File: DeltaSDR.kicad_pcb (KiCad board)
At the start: 2 copper layers, 168 parts, among them J1 Conn_01x03_Male, J2 Conn_01x05_Male, J3 Barrel_Jack, J4 USB_A, J5 Conn_Coaxial, Q1 BSS123, Q2 BSS123, Q3 BSS123, Q4 BSS123, Q5 BSS123, Q6 BSS123, T1 Transformer_1P_SS, T2 Transformer_1P_SS, U1 TC1262-33, U10 TLV2464CD, U11 SN74CBT3253, U12 MMG3H21NT1, U2 Si570, U3 SN74CBT3253, U4 PCM3060, U5 CY8C3246PVI-147, U6 TLV761, U7 TLV761, U8 74HC74, U9 LT6231CSB, Y1 Crystal_GND24

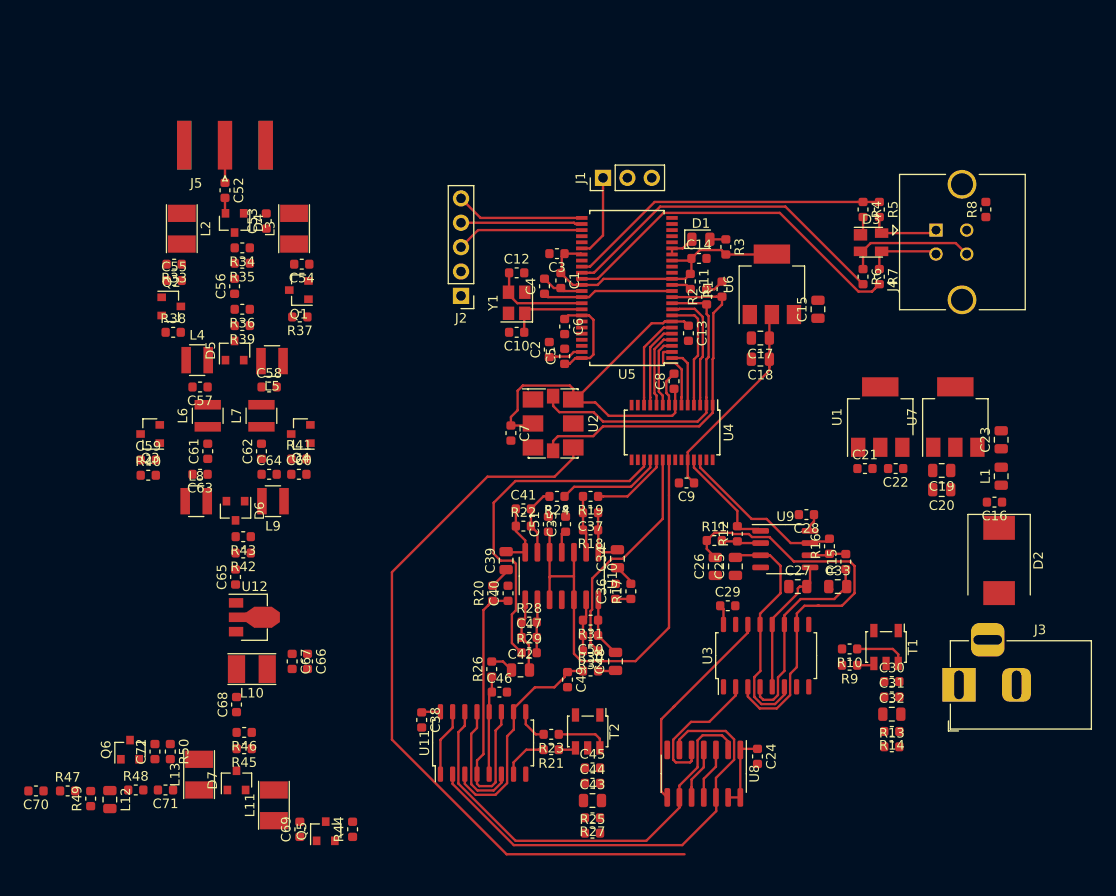
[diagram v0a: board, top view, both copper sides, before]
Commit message: Layout: All components connected
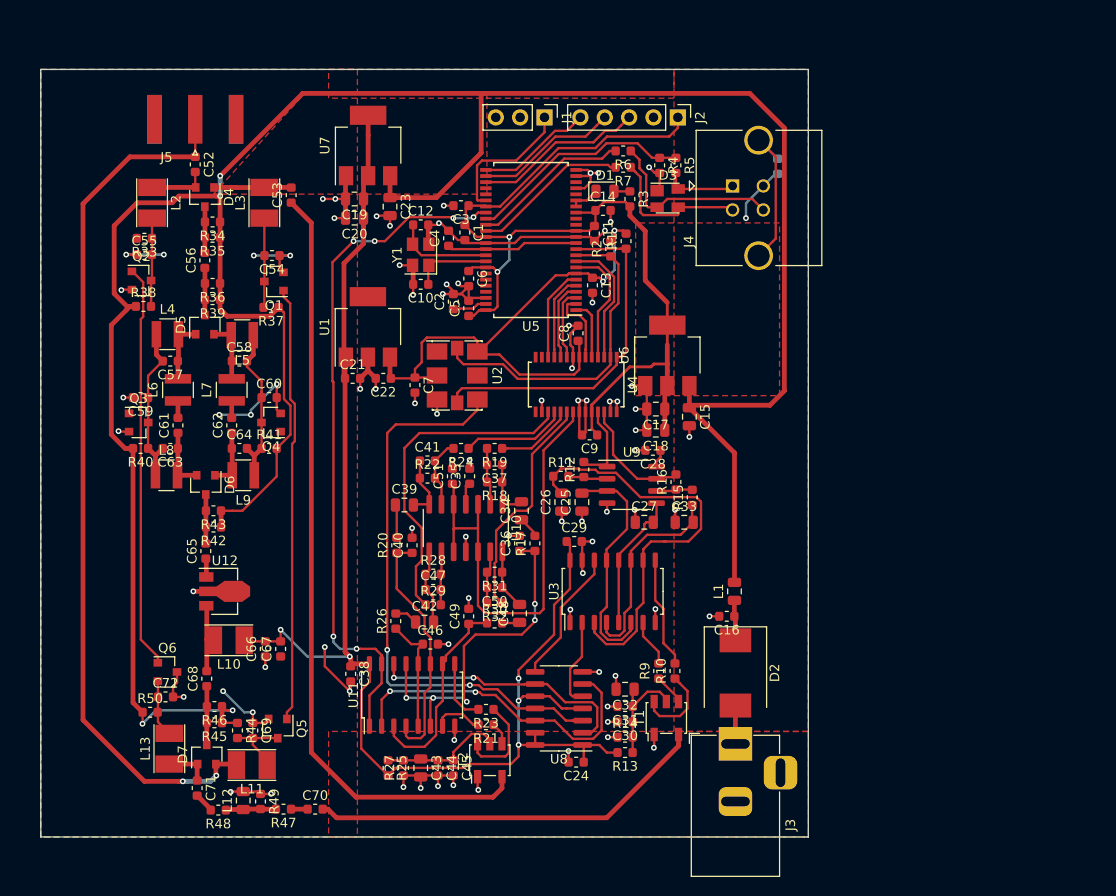
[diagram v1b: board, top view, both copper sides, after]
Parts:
- R8: moved to B.Cu
- moved C23 68.2 mm to (141.4, 79.3), turned to 270 degrees
- moved C19 67.4 mm to (137.7, 78.5)
- moved C20 67.4 mm to (137.7, 80.5)
- moved U7 67.4 mm to (139.1, 72.9)
- moved U1 54.2 mm to (139.1, 91.8)
- moved C21 54.2 mm to (137.5, 97.2)
- moved C22 54.2 mm to (140.7, 97.2)
- moved C16 30.3 mm to (176.5, 122.0)
- moved L1 30.3 mm to (177.3, 119.4)
- moved D2 29.9 mm to (177.4, 127.9)
- moved J2 29.3 mm to (171.4, 70.0), turned to 270 degrees
- moved C70 29.2 mm to (133.6, 142.1), turned to 0 degrees
- moved R7 29.0 mm to (165.7, 75.2), turned to 180 degrees
- moved R6 28.2 mm to (165.7, 73.5), turned to 180 degrees
- moved C30 28.1 mm to (165.9, 133.0), turned to 180 degrees
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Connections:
- C53 pad 1: TX_OUT -> TXOUT
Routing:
- net +12V: track 0.00 -> 276.2 mm, vias 0 -> 4
- net GND: track 14.2 -> 203.2 mm, vias 2 -> 84
- net +5V: track 17.6 -> 150.0 mm, vias 0 -> 5
- net PA_IN: track 3.91 -> 91.6 mm, vias 0 -> 2
- net TXOUT: track 0.00 -> 81.6 mm
- net RX: track 7.03 -> 71.4 mm, vias 0 -> 6
- net HI_TX: track 0.00 -> 45.5 mm
- net HI_RX: track 0.00 -> 42.2 mm
- net RX_RF: track 0.00 -> 41.8 mm
- net +5VD: track 63.1 -> 103.5 mm, vias 0 -> 2
- net Net-(U2-Pad4): track 83.3 -> 59.5 mm, vias 0 -> 2
- net Net-(C36-Pad1): track 14.0 -> 36.4 mm, vias 0 -> 5
- net USB-: track 37.6 -> 16.5 mm
- net QSE_Q: track 47.1 -> 27.8 mm, vias 0 -> 2
- net USB+: track 35.5 -> 16.7 mm
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- added copper zone on F.Cu, net +5V
- added copper zone on F.Cu, net +5VD
- added copper zone on B.Cu, net GND
- added copper zone on F.Cu, net GND
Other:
- board outline added: 80 x 80 mm

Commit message: Changed RF front end layout
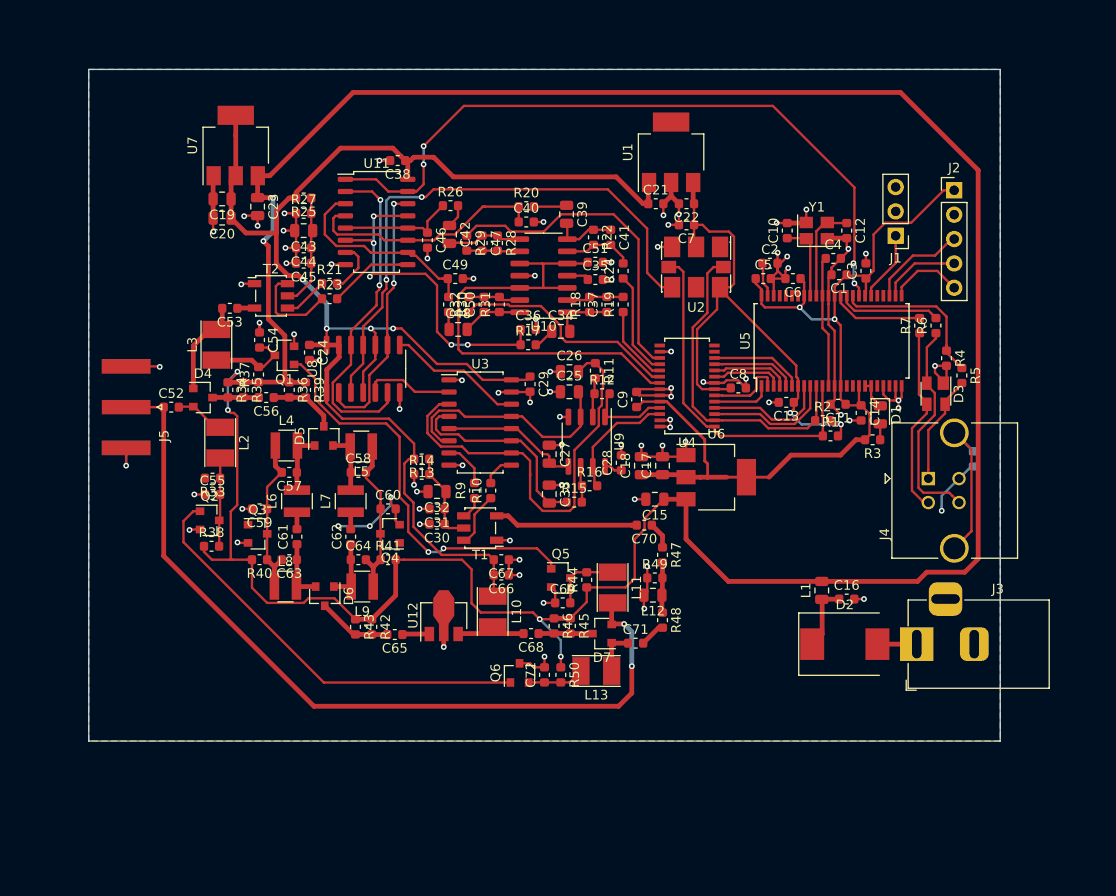
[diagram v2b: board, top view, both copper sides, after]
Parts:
- moved R25 60.0 mm to (132.4, 78.4), turned to 180 degrees
- moved R27 58.7 mm to (132.4, 80.0), turned to 0 degrees
- moved C43 57.3 mm to (132.4, 81.8), turned to 180 degrees
- moved C44 56.0 mm to (132.4, 83.6), turned to 180 degrees
- moved C45 54.9 mm to (132.4, 85.2), turned to 180 degrees
- moved C38 53.7 mm to (142.2, 74.5), turned to 180 degrees
- moved T2 53.5 mm to (129.0, 88.6), turned to 0 degrees
- moved C24 51.0 mm to (133.0, 94.5), turned to 270 degrees
- moved R48 50.4 mm to (169.8, 122.4), turned to 270 degrees
- moved U11 49.4 mm to (140.0, 80.9), turned to 0 degrees
- moved R21 48.8 mm to (135.1, 87.3), turned to 0 degrees
- moved C71 48.1 mm to (167.0, 124.8), turned to 0 degrees
- moved L12 47.8 mm to (168.8, 119.8), turned to 180 degrees
- moved R47 47.6 mm to (169.8, 115.6), turned to 270 degrees
- moved R49 47.2 mm to (169.0, 118.0), turned to 0 degrees
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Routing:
- net TXOUT: track 81.6 -> 1.81 mm
- net RX_RF: track 41.8 -> 15.0 mm
- net +12V: track 276.2 -> 295.4 mm, vias 4 -> 6
- net +5VD: track 103.5 -> 94.3 mm
- net +5V: track 150.0 -> 158.4 mm, vias 5 -> 4
- net Net-(R10-Pad2): track 11.6 -> 3.40 mm
- net RES: track 17.7 -> 10.2 mm
- net GND: track 203.2 -> 195.7 mm, vias 84 -> 82
- net BOOT: track 14.5 -> 7.31 mm
- net USB-: track 16.5 -> 9.63 mm
- net SWDCLK: track 14.9 -> 8.32 mm
- net USBV+: track 23.7 -> 17.1 mm
- net USB+: track 16.7 -> 10.7 mm
- net PA_IN: track 91.6 -> 86.4 mm
- net Net-(D3-Pad3): track 15.7 -> 20.1 mm
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- removed copper zone on F.Cu, net +5V
- removed copper zone on F.Cu, net +5VD
- removed copper zone on F.Cu, net GND
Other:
- board size 80 x 80 mm -> 95 x 70 mm

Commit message: Added remaining switching signals and polygons
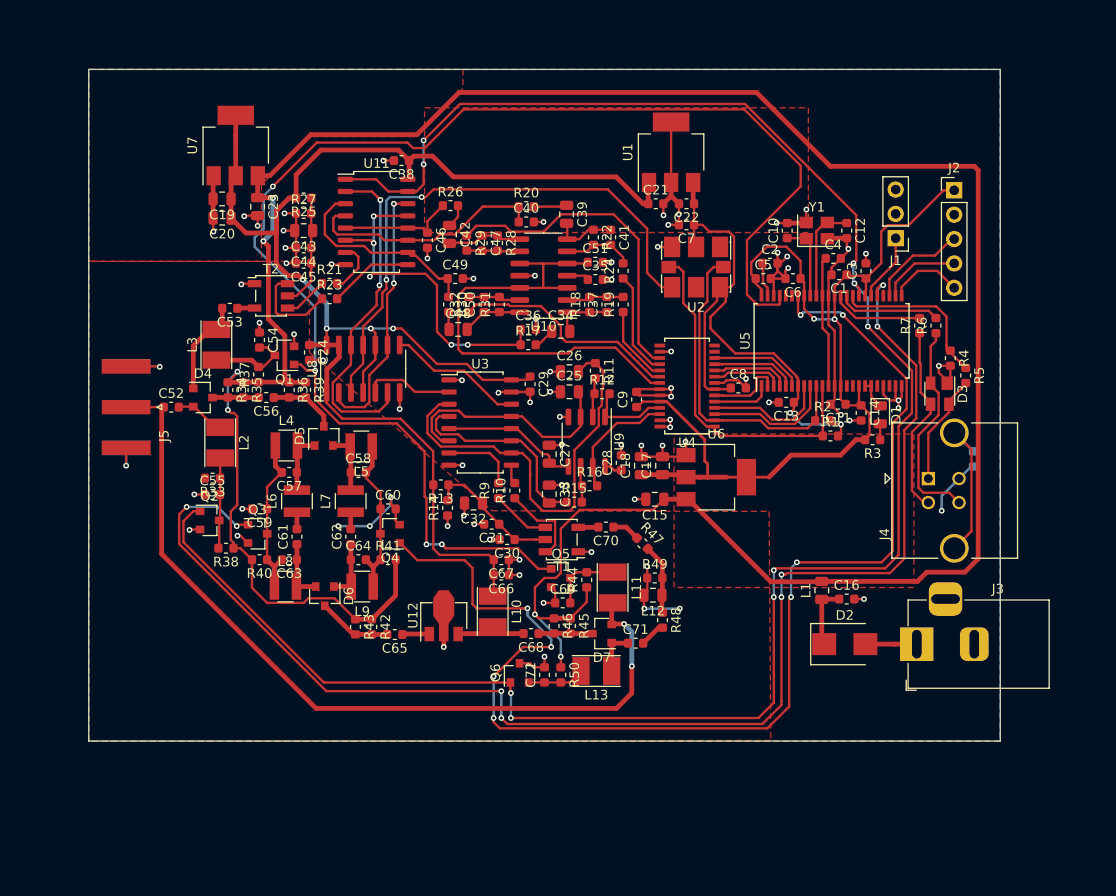
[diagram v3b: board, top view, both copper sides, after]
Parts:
- D2: footprint Diode_SMD:D_SMC -> Diode_SMD:D_SMB
- moved T1 8.58 mm to (159.3, 114.0)
- moved C30 7.47 mm to (153.6, 114.0)
- moved C31 5.92 mm to (152.0, 112.4)
- moved R14 4.42 mm to (147.4, 110.7), turned to 90 degrees
- moved C70 4.00 mm to (163.9, 112.7)
- moved C32 3.98 mm to (150.1, 110.2)
- moved R13 3.36 mm to (146.7, 108.3)
- moved R10 2.50 mm to (154.4, 108.9)
- moved R9 2.50 mm to (152.7, 108.9)
- moved R47 2.42 mm to (167.7, 114.4), turned to 315 degrees
- moved R38 1.51 mm to (124.3, 114.9), turned to 180 degrees
- moved C38 0.40 mm to (142.6, 74.5)
- moved R4 0.40 mm to (199.8, 95.1)
- moved R5 0.40 mm to (201.4, 96.9)
- moved D3 0.40 mm to (198.7, 98.8)
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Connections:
- U11 pad 1: RX -> HI_RX
- U11 pad 15: RX -> HI_RX
- U5 pad 29: Net-(U5-Pad29) -> B6040M
- U5 pad 32: RX -> HI_RX
- U5 pad 42: XK -> B80M
- U5 pad 45: TX -> HI_TX
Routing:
- net HI_RX: track 44.5 -> 208.9 mm, vias 0 -> 9
- net B6040M: track 0.00 -> 144.1 mm, vias 0 -> 8
- net B80M: track 0.00 -> 128.0 mm, vias 0 -> 8
- net HI_TX: track 42.8 -> 147.2 mm, vias 2 -> 4
- net RX: track 74.7 -> 0.00 mm, vias 4 -> 0
- net +12V: track 295.4 -> 278.0 mm
- net RX_RF: track 15.0 -> 2.11 mm
- net GND: track 195.7 -> 205.3 mm
- net Net-(C30-Pad1): track 9.75 -> 14.6 mm
- net +5VD: track 94.3 -> 98.6 mm
- net Net-(R9-Pad1): track 2.42 -> 6.15 mm
- net Net-(R10-Pad1): track 5.74 -> 9.00 mm
- net Net-(R9-Pad2): track 4.85 -> 7.75 mm
- net +3V3: track 58.5 -> 61.1 mm
- net Net-(L12-Pad1): track 5.28 -> 7.34 mm
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- added copper zone on F.Cu, net +5V
- added copper zone on F.Cu, net +5VD
- added copper zone on F.Cu, net GND

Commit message: Changed board size, changed PA_IN signal position, changed LDOs, added 50 ohm tracks andvias
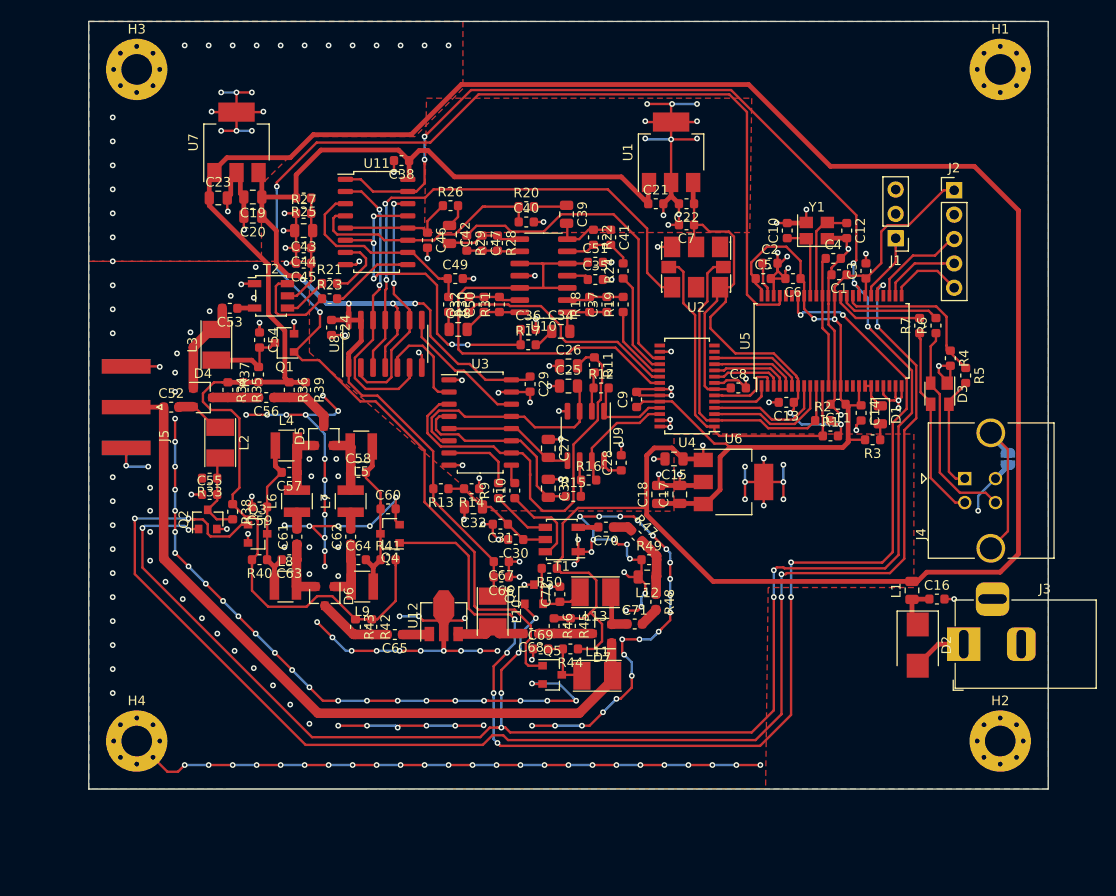
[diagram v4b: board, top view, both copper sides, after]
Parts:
- removed R8: 0R, Resistor_SMD:R_0603_1608Metric
- added H1: MountingHole_Pad, MountingHole:MountingHole_3.2mm_M3_Pad_Via, F.Cu at (205.0, 65.0)
- added H2: MountingHole_Pad, MountingHole:MountingHole_3.2mm_M3_Pad_Via, F.Cu at (205.0, 135.0)
- added H3: MountingHole_Pad, MountingHole:MountingHole_3.2mm_M3_Pad_Via, F.Cu at (115.0, 65.0)
- added H4: MountingHole_Pad, MountingHole:MountingHole_3.2mm_M3_Pad_Via, F.Cu at (115.0, 135.0)
- added JP1: Jumper, Jumper:SolderJumper-2_P1.3mm_Open_RoundedPad1.0x1.5mm, B.Cu at (205.8, 105.6)
- U6, U7: value TLV761 -> TC1262-5
- moved R50 11.2 mm to (158.0, 117.0), turned to 180 degrees
- moved Q5 10.1 mm to (158.3, 128.1)
- moved C16 9.40 mm to (198.4, 120.2)
- moved L1 9.40 mm to (195.8, 119.3)
- moved L11 9.34 mm to (163.0, 128.2), turned to 0 degrees
- moved C72 8.55 mm to (159.1, 119.7)
- moved Q6 8.34 mm to (156.4, 119.7)
- moved L13 8.21 mm to (162.8, 119.5)
- moved D2 7.60 mm to (196.4, 125.0), turned to 270 degrees
- moved R44 7.40 mm to (160.2, 125.4), turned to 180 degrees
- moved C69 5.32 mm to (157.1, 125.4)
- moved J3 4.90 mm to (201.2, 124.9)
- moved C15 4.65 mm to (171.0, 105.6)
- moved C23 4.20 mm to (123.5, 78.4), turned to 0 degrees
- moved R38 3.86 mm to (125.0, 111.1), turned to 270 degrees
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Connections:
- D7 pad 1: Net-(C71-Pad1) -> PA_IN
- D7 pad 2: PA_IN -> Net-(C71-Pad1)
- U1 pad 4: (no net) -> GND
- U6 pad 1: GND -> +12V
- U6 pad 2: +5VD -> GND
- U6 pad 3: +12V -> +5VD
- U6 pad 4: +5VD -> GND
- U7 pad 1: GND -> +12V
- U7 pad 2: +5V -> GND
- U7 pad 3: +12V -> +5V
- U7 pad 4: +5V -> GND
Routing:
- net GND: track 205.3 -> 526.4 mm, vias 82 -> 278
- net +12V: track 278.0 -> 303.9 mm, vias 6 -> 1
- net HI_RX: track 208.9 -> 234.7 mm, vias 9 -> 13
- net +5V: track 159.0 -> 143.5 mm
- net B6040M: track 144.1 -> 156.6 mm, vias 8 -> 6
- net PA_IN: track 86.8 -> 78.5 mm, vias 2 -> 0
- net QSE_J: track 34.8 -> 30.8 mm
- net Net-(U2-Pad4): track 58.7 -> 55.1 mm
- net QSE_Q: track 27.8 -> 25.5 mm
- net Net-(C72-Pad1): track 5.95 -> 8.12 mm
- net Net-(C30-Pad1): track 14.6 -> 12.5 mm
- net Net-(C16-Pad1): track 6.43 -> 4.53 mm
- net B80M: track 128.0 -> 126.3 mm
- net Net-(C27-Pad2): track 14.5 -> 13.0 mm
- net QSD_J: track 9.37 -> 10.8 mm
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- removed copper zone on F.Cu, net +5V
- removed copper zone on F.Cu, net +5VD
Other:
- board size 95 x 70 mm -> 100 x 80 mm
- net class 50ohm added: clearance 0.15, trace_width 1, via_dia 0.6, via_drill 0.3

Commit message: Changed connectors position, ground separation, added lot of vias
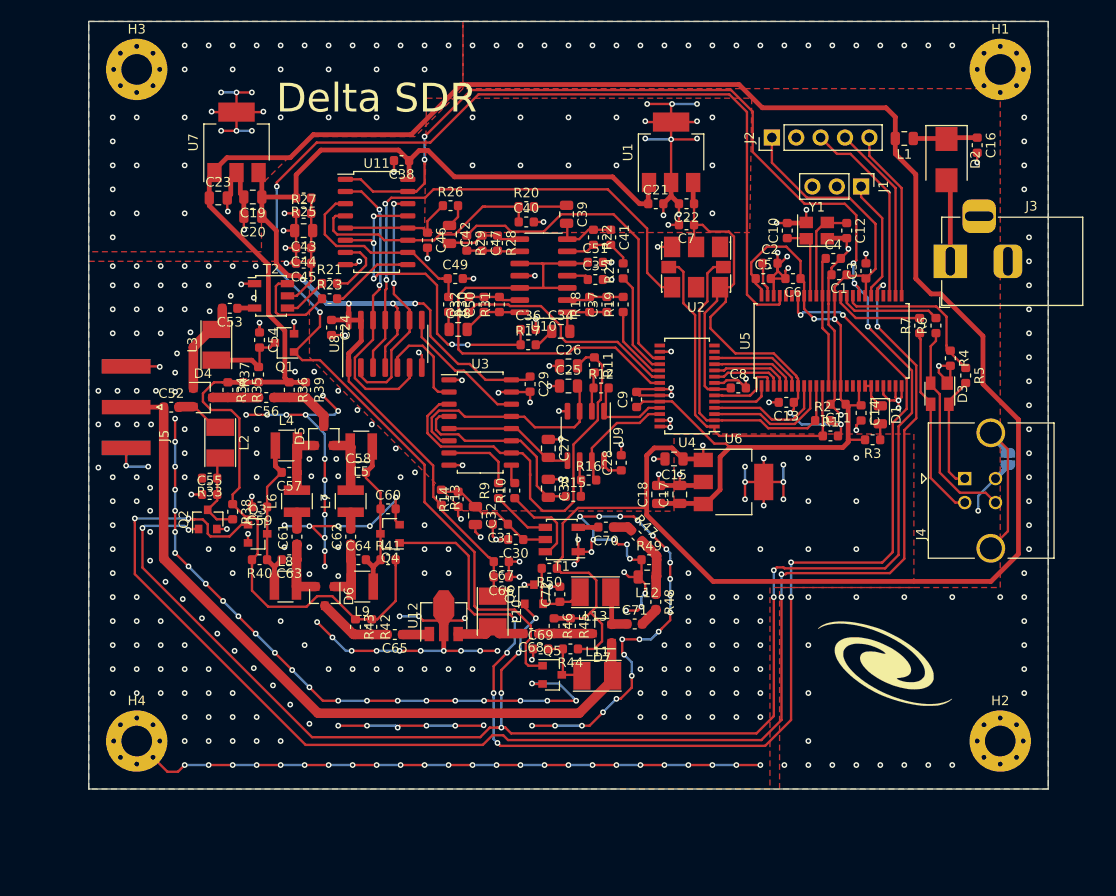
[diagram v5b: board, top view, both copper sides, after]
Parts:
- added G***: RiskeLogo, riske-lib:RiskeLogo, F.Cu at (193.0, 127.0)
- moved D2 50.7 mm to (199.4, 74.4)
- moved C16 47.5 mm to (202.6, 72.9), turned to 270 degrees
- moved L1 47.1 mm to (195.0, 72.2), turned to 180 degrees
- moved J3 39.9 mm to (199.8, 85.0)
- moved J2 19.8 mm to (181.2, 72.1), turned to 90 degrees
- moved J1 6.49 mm to (190.5, 77.2), turned to 270 degrees
- moved R14 1.78 mm to (148.5, 109.8), turned to 90 degrees
- moved C32 0.92 mm to (150.3, 111.5), turned to 270 degrees
- moved R13 0.90 mm to (146.8, 109.6), turned to 270 degrees
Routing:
- net SWDCLK: track 8.32 -> 18.7 mm
- net SWDIO: track 7.81 -> 17.9 mm
- net RES: track 10.2 -> 20.3 mm
- net +5VD: track 98.8 -> 106.1 mm
- net BOOT: track 7.31 -> 12.8 mm
- net HI_RX: track 234.7 -> 237.6 mm
- net Net-(D2-Pad2): track 5.79 -> 8.62 mm
- net Net-(C16-Pad1): track 4.53 -> 6.74 mm
- net +12V: track 303.9 -> 302.7 mm
- net HI_TX: track 146.9 -> 146.1 mm
- net +5V: track 143.5 -> 142.9 mm
- net GND: track 526.4 -> 526.0 mm, vias 278 -> 484
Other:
- board text added: "Delta SDR"

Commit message: Improved ground separation and silk screen
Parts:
- added G***: LOGO, riske-lib:DeltaSymbol, B.Cu at (132.8, 84.4)
- moved L1 3.88 mm to (197.2, 69.0)
- moved G*** 2.80 mm to (190.2, 127.0)
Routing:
- net GND: track 526.0 -> 531.7 mm, vias 484 -> 491
- net +12V: track 302.7 -> 304.6 mm
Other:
- board text added: "200413"
